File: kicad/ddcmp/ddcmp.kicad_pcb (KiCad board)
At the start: 2 copper layers, 29 parts, among them J1 UART, J2 BNC, J3 BNC, J4 LOOPTEST, U1 Pico, U2 max3089ecpd, U3 MAX3222, U4 MAX3222

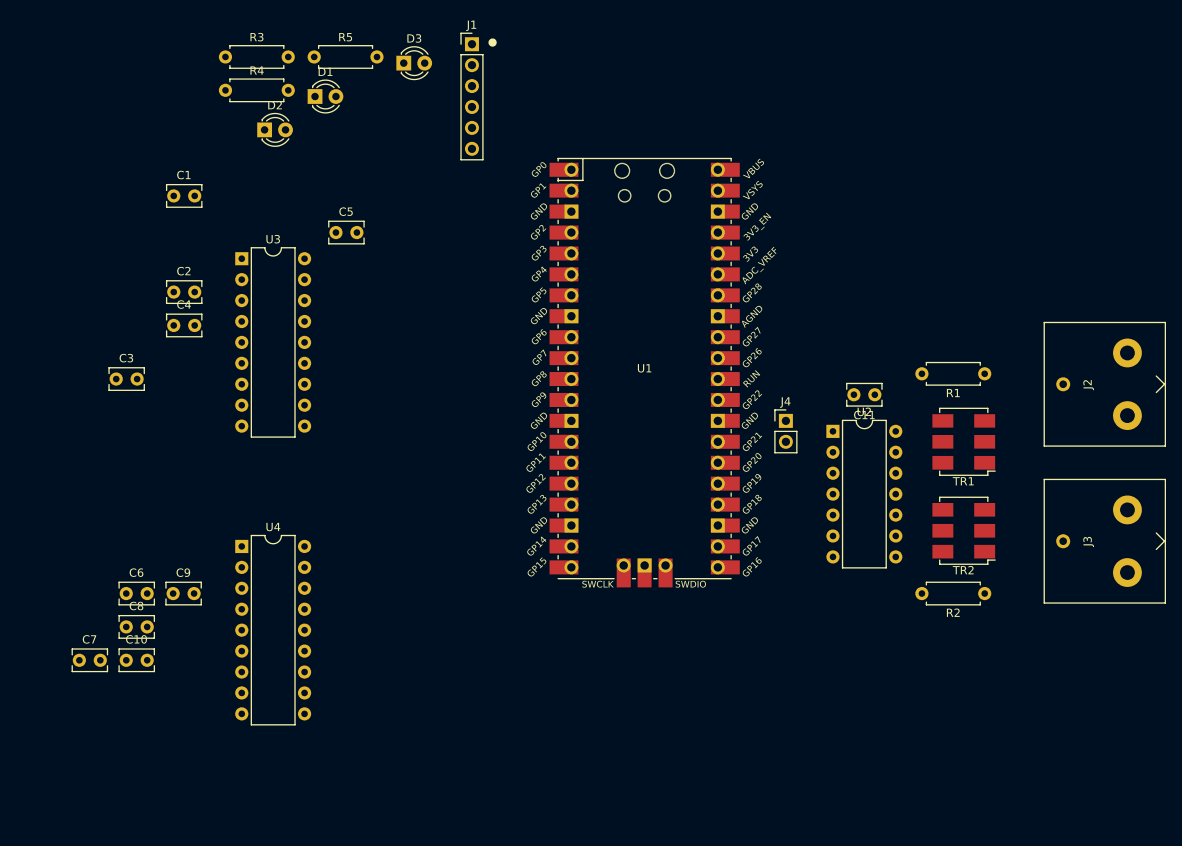
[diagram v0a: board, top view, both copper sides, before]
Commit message: Finish the connector hookups, to be verified carefully against DMR-11 schematics.
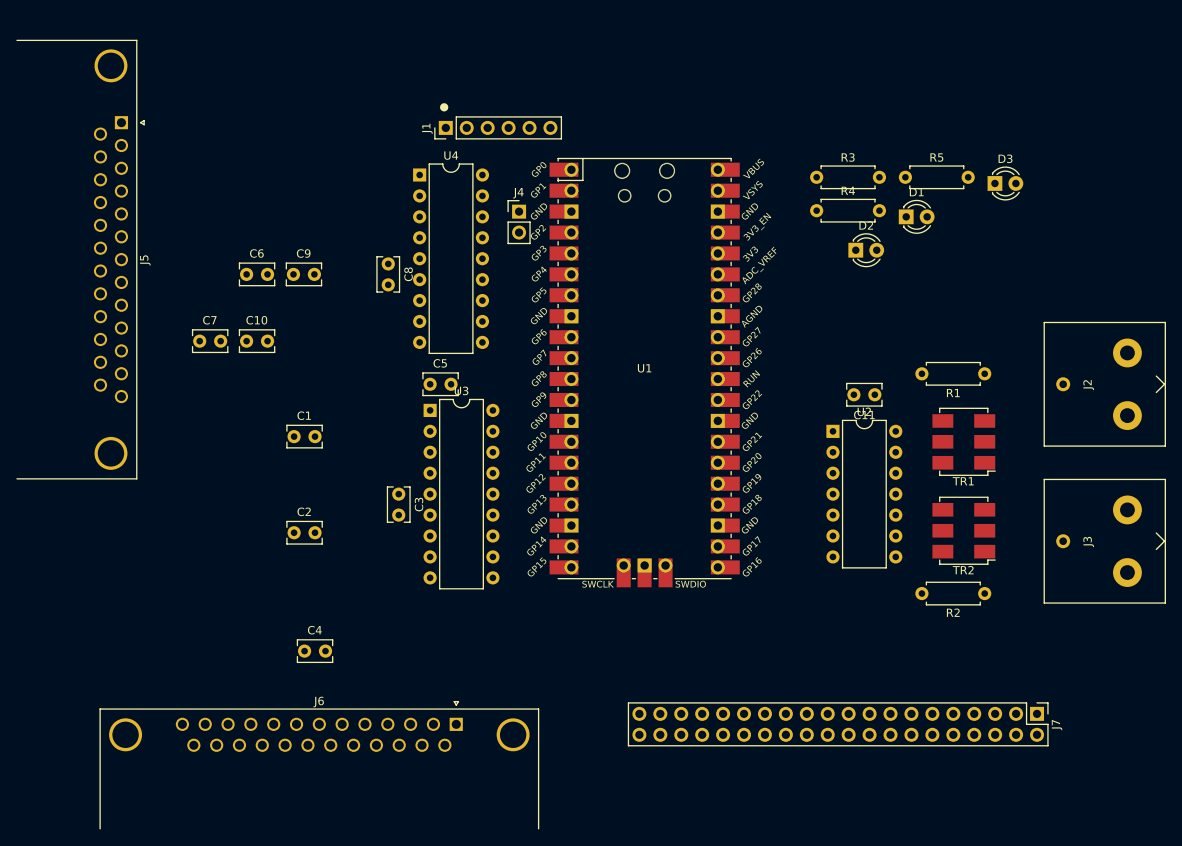
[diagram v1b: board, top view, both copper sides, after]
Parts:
- added J5: DTE, ddcmp_parts:Amphenol_DB25M_PCB, F.Cu at (29.2, 100.3)
- added J6: DCE, ddcmp_parts:Amphenol_DB25F_PCB, F.Cu at (69.8, 173.4)
- added J7: Bulkhead, ddcmp_parts:Berg_40_pin_DEC_pinout, F.Cu at (140.3, 172.1)
- J2: value BNC -> RX
- J3: value BNC -> TX
- moved D1 73.2 mm to (124.5, 111.8)
- moved D2 73.2 mm to (118.3, 115.8)
- moved D3 73.2 mm to (135.2, 107.7)
- moved R3 73.2 mm to (113.6, 107.0)
- moved R4 73.2 mm to (113.6, 111.0)
- moved R5 73.2 mm to (124.4, 107.0)
- moved C8 54.3 mm to (61.6, 117.5), turned to 270 degrees
- moved U4 50.0 mm to (65.4, 106.7)
- moved C4 42.6 mm to (51.4, 164.5)
- moved C10 41.4 mm to (44.4, 126.8)
- moved C7 41.4 mm to (38.7, 126.8)
- moved C9 41.4 mm to (50.1, 118.7)
- moved C6 41.4 mm to (44.4, 118.7)
- moved J4 41.2 mm to (77.5, 111.1)
- moved C3 37.0 mm to (62.9, 145.4), turned to 270 degrees
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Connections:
- net Net-(J2-Pad1) renamed /Integral modem/IM_RDX
- net Net-(J2-Pad2) renamed /Integral modem/IM_RXD_N
- net Net-(J3-Pad1) renamed /Integral modem/IM_TDX
- net Net-(J3-Pad2) renamed /Integral modem/IM_TXD_N
- TR2 pad 5: GND -> Net-(TR2-Pad5)
- U1 pad 12: /CPU/RS232_CLKEN -> Net-(U1-Pad12)
- U1 pad 21: /CPU/IM_RXDATA -> /CPU/IM_SRL
- U1 pad 25: /CPU/IM_SRL -> /CPU/IM_RXDATA
- U1 pad 26: Net-(U1-Pad26) -> Net-(D1-Pad2)
- U1 pad 27: Net-(J4-Pad2) -> Net-(D2-Pad2)
- U1 pad 29: Net-(U1-Pad29) -> Net-(D3-Pad2)
- U1 pad 4: Net-(D1-Pad2) -> Net-(J4-Pad2)
- U1 pad 5: Net-(D2-Pad2) -> Net-(U1-Pad5)
- U1 pad 6: Net-(D3-Pad2) -> Net-(U1-Pad6)
- U3 pad 14: Net-(U3-Pad14) -> /RS-232 I/O/RXD
- U3 pad 15: Net-(U3-Pad15) -> /RS-232 I/O/RS232_1
- U3 pad 8: Net-(U3-Pad8) -> /RS-232 I/O/TXD
- U4 pad 14: Net-(U4-Pad14) -> /RS-232 I/O/RXCLK
- U4 pad 15: Net-(U4-Pad15) -> /RS-232 I/O/CLKOUT
- U4 pad 18: /CPU/RS232_CLKEN -> /CPU/RS232_ENABLE
- U4 pad 8: Net-(U4-Pad8) -> /RS-232 I/O/RS232_0
- U4 pad 9: Net-(U4-Pad9) -> /RS-232 I/O/TXCLK

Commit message: Complete schematic, PCB layout, and matching code.  Needs testing.
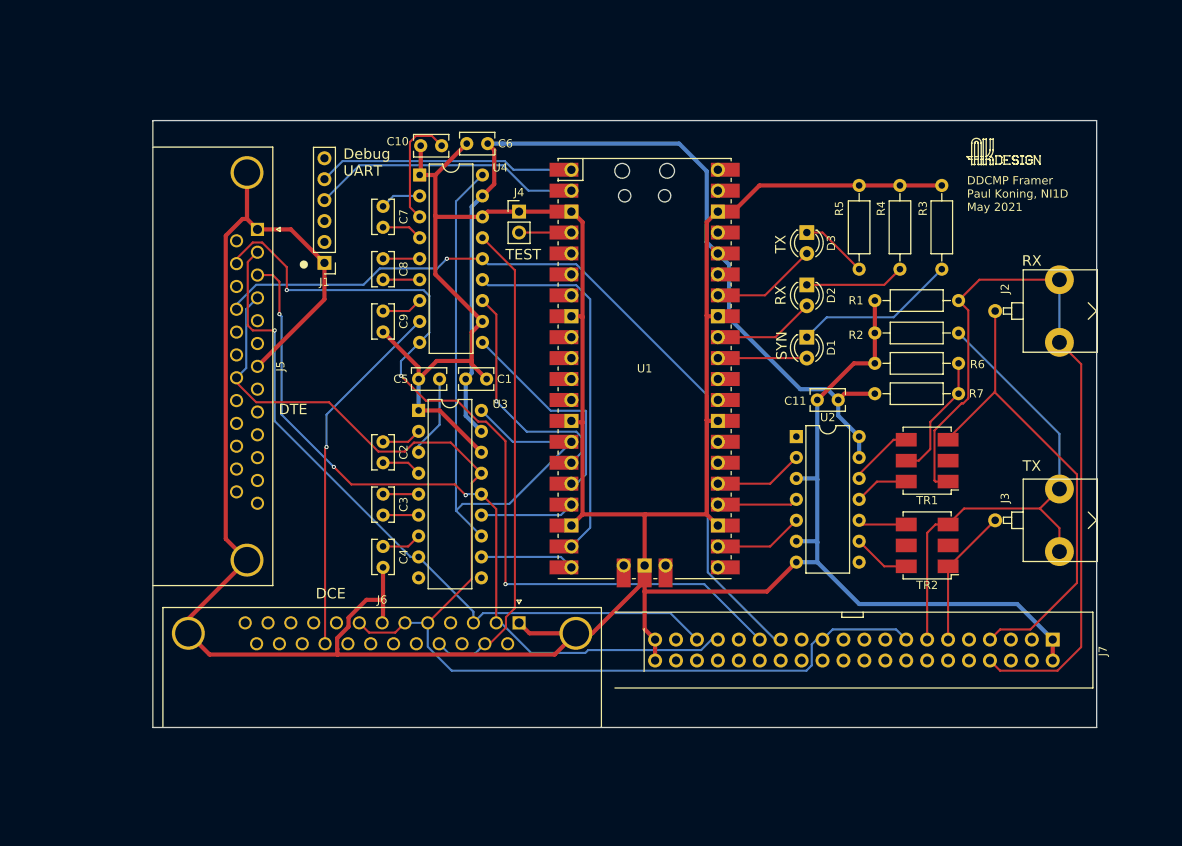
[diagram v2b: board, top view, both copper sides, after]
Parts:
- added R6: 240, ddcmp_parts:R_Axial_DIN0207_L6.3mm_D2.5mm_P10.16mm_Horizontal, F.Cu at (120.7, 133.2)
- added R7: 750, ddcmp_parts:R_Axial_DIN0207_L6.3mm_D2.5mm_P10.16mm_Horizontal, F.Cu at (130.8, 129.5)
- added REF**: AK_Design_9mm, ddcmp_parts:AK_Design_9mm, F.Cu at (131.8, 105.4)
- D1: value LED -> SYN; footprint LEDs:LED_D3.0mm -> ddcmp_parts:LED_D3.0mm
- D2: value LED -> RX; footprint LEDs:LED_D3.0mm -> ddcmp_parts:LED_D3.0mm
- D3: value LED -> TX; footprint LEDs:LED_D3.0mm -> ddcmp_parts:LED_D3.0mm
- J4: value LOOPTEST -> TEST; footprint Pin_Headers:Pin_Header_Straight_1x02_Pitch2.54mm -> ddcmp_parts:Pin_Header_Straight_1x02_Pitch2.54mm
- R1, R2, R3, R4, R5: footprint ddcmp_parts:R_Axial_DIN0207_L6.3mm_D2.5mm_P7.62mm_Horizontal -> ddcmp_parts:R_Axial_DIN0207_L6.3mm_D2.5mm_P10.16mm_Horizontal
- U2: value max3089ecpd -> max3491ecpd
- moved C10 33.5 mm to (68.1, 103.1), turned to 180 degrees
- moved C6 33.3 mm to (73.7, 102.9), turned to 180 degrees
- moved R2 31.8 mm to (130.8, 125.9)
- moved C7 27.6 mm to (61.0, 110.5), turned to 270 degrees
- moved D3 23.6 mm to (112.4, 113.7), turned to 270 degrees
- moved J1 22.0 mm to (53.8, 117.3), turned to 180 degrees
- moved C1 22.0 mm to (71.0, 131.4)
- moved J5 21.0 mm to (45.7, 113.3)
- moved D1 18.9 mm to (112.4, 126.4), turned to 270 degrees
- moved R3 18.8 mm to (128.8, 118.1), turned to 90 degrees
- moved C4 15.9 mm to (61.0, 151.8), turned to 270 degrees
- moved C2 15.4 mm to (61.0, 139.1), turned to 270 degrees
- moved J6 14.5 mm to (77.5, 161.0)
- moved R5 12.5 mm to (118.7, 118.1), turned to 90 degrees
- moved R4 12.4 mm to (123.7, 118.1), turned to 90 degrees
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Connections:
- J5 pad 15: /RS-232 I/O/CLKOUT -> /RS-232 I/O/TXCLK
- J5 pad 17: /RS-232 I/O/CLKOUT -> /RS-232 I/O/RXCLK
- J6 pad 15: /RS-232 I/O/TXCLK -> /RS-232 I/O/CLKOUT
- J6 pad 17: /RS-232 I/O/RXCLK -> /RS-232 I/O/CLKOUT
- U1 pad 21: /CPU/IM_SRL -> Net-(U1-Pad21)
- U1 pad 26: Net-(D1-Pad2) -> Net-(U1-Pad26)
- U1 pad 27: Net-(D2-Pad2) -> Net-(U1-Pad27)
- U1 pad 29: Net-(D3-Pad2) -> Net-(U1-Pad29)
- U1 pad 31: Net-(U1-Pad31) -> Net-(D1-Pad2)
- U1 pad 32: Net-(U1-Pad32) -> Net-(D2-Pad2)
- U1 pad 34: Net-(U1-Pad34) -> Net-(D3-Pad2)
- U2 pad 1: GND -> (no net)
- U2 pad 13: GND -> V3_3
- U2 pad 6: /CPU/IM_SRL -> GND
- U2 pad 8: GND -> (no net)
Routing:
- net GND: track 0.00 -> 504.6 mm
- net /RS-232 I/O/RS232_1: track 0.00 -> 142.9 mm
- net V3_3: track 0.00 -> 114.6 mm
- net /RS-232 I/O/TXCLK: track 0.00 -> 107.5 mm, vias 0 -> 3
- net /RS-232 I/O/RXCLK: track 0.00 -> 101.0 mm, vias 0 -> 1
- net /Integral modem/IM_RXD_N: track 0.00 -> 97.6 mm
- net /RS-232 I/O/RXD: track 0.00 -> 93.3 mm, vias 0 -> 3
- net /RS-232 I/O/TXD: track 0.00 -> 88.0 mm, vias 0 -> 1
- net /CPU/RS232_ENABLE: track 0.00 -> 76.4 mm
- net /Integral modem/IM_TXD_N: track 0.00 -> 61.4 mm
- net /RS-232 I/O/CLKOUT: track 0.00 -> 59.3 mm
- net /Integral modem/IM_RDX: track 0.00 -> 58.7 mm
- net /CPU/RS232_RXCLK: track 0.00 -> 45.0 mm
- net /RS-232 I/O/RS232_0: track 0.00 -> 43.9 mm, vias 0 -> 1
- net Net-(J1-Pad4): track 0.00 -> 33.0 mm
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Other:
- board outline added: 114.6 x 73.7 mm
- net class Default: clearance 0.2 -> 0.254; trace_width 0.25 -> 0.254; via_dia 0.8 -> 0.508; via_drill 0.4 -> 0.254
- net class Power added: clearance 0.254, trace_width 0.508, via_dia 0.508, via_drill 0.254
- rule pad_to_mask_clearance: 0 -> 0.0508
- rule trace_clearance: 0.2 -> 0.254
- rule trace_min: 0.2 -> 0.1524
- rule via_min_drill: 0.3 -> 0.254
- rule via_min_size: 0.4 -> 0.508
- board text added: "DCE"
- board text added: "DDCMP Framer Paul Koning, NI1D May 2021"
- board text added: "DTE"
- board text added: "Debug UART"
- board text added: "RX"
- board text added: "SYN"
- board text added: "TEST"
- board text added: "TX"

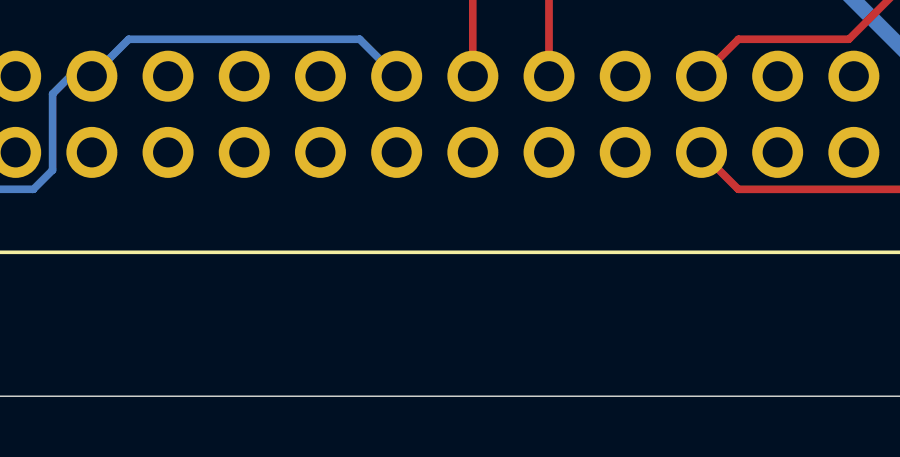
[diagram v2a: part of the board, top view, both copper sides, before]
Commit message: Schematics tweaks, better 3d model for RPico.
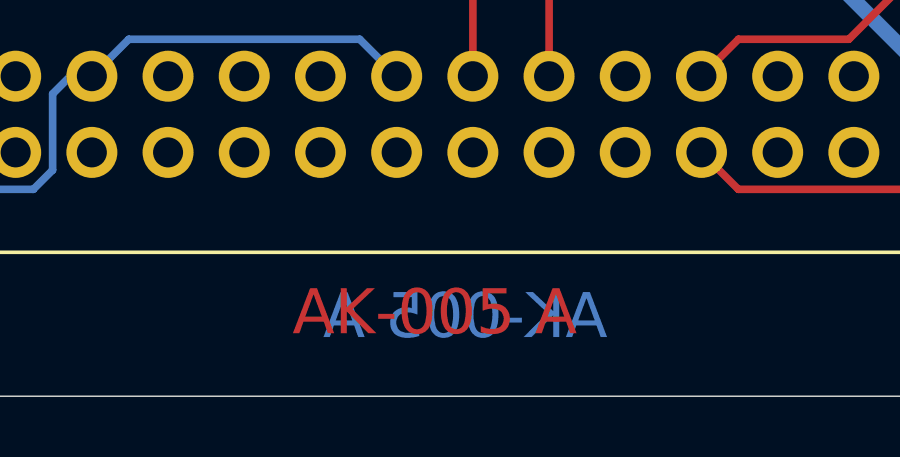
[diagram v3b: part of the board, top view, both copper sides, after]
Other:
- board text added: "AK-005 A"

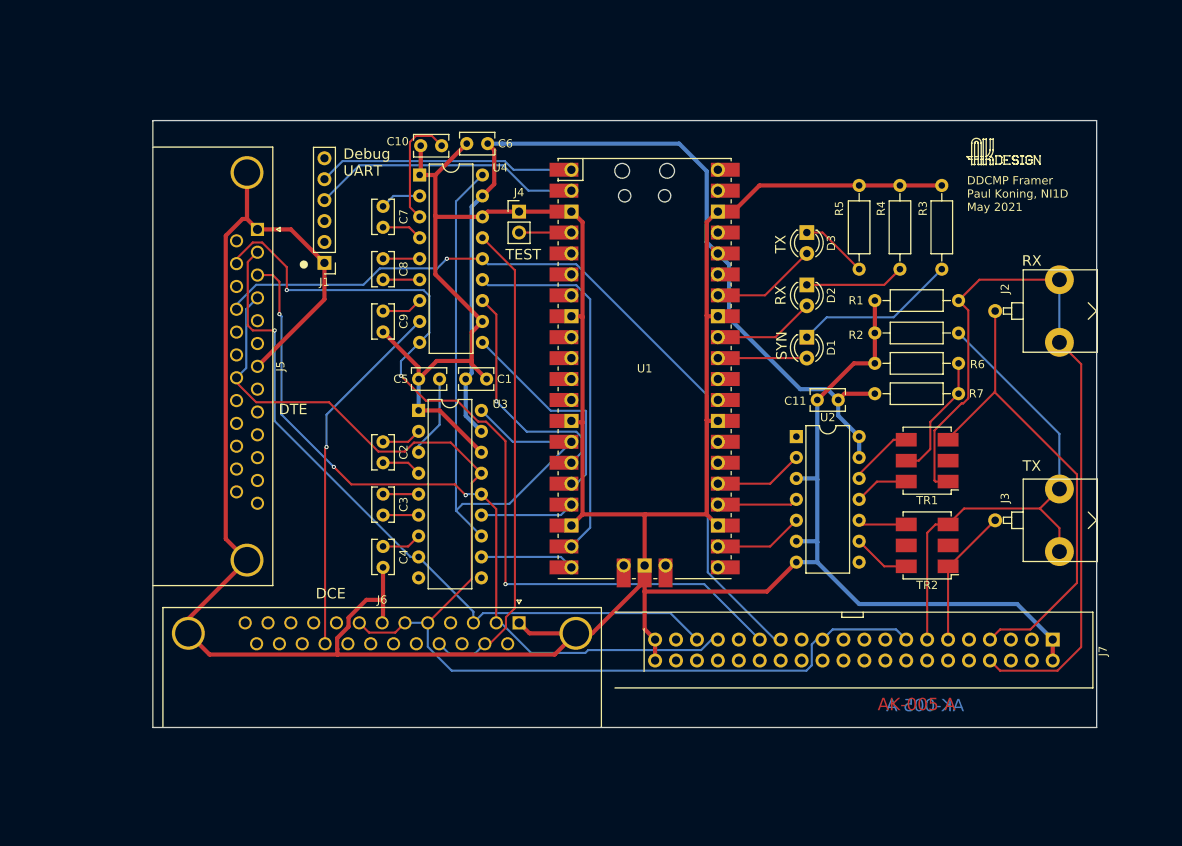
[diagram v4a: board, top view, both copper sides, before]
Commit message: Schematics and 3d model cleanups; first drafts of a lot of documentation.
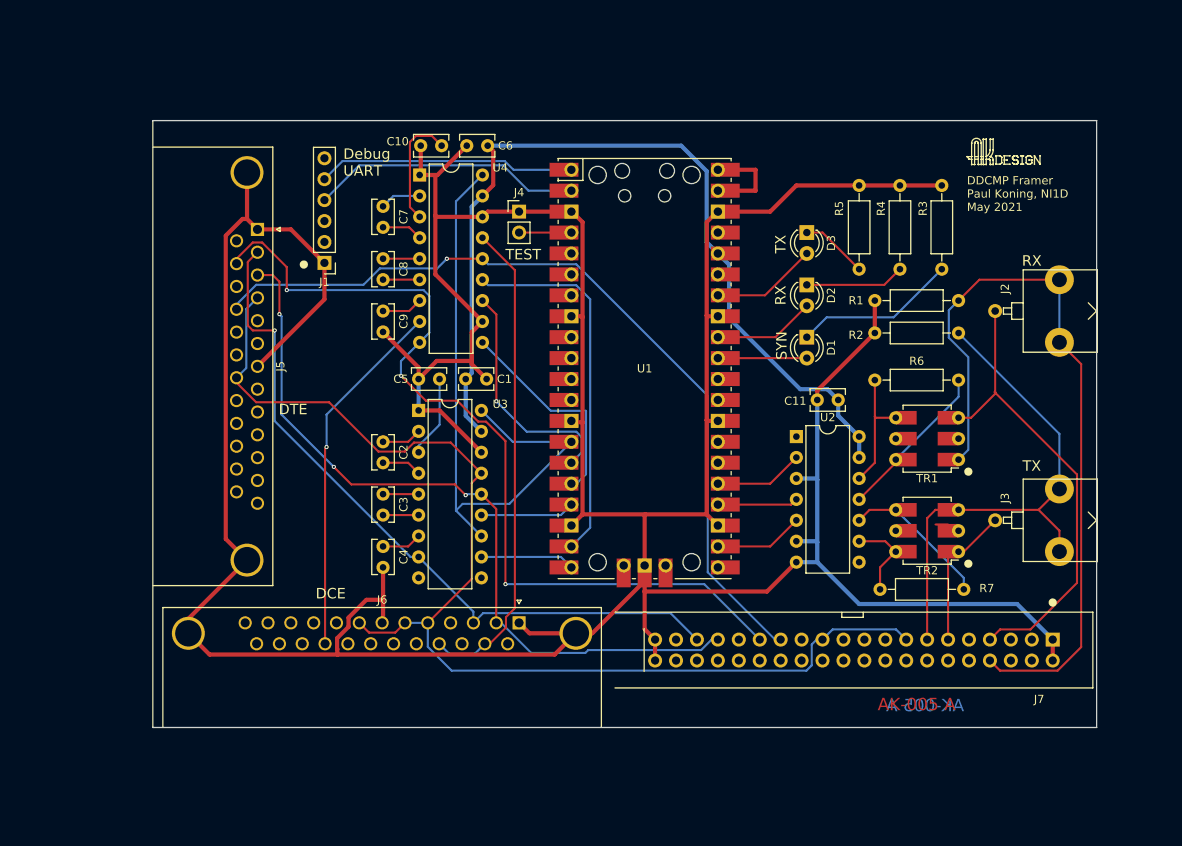
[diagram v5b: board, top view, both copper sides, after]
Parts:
- R6: value 240 -> 51
- R7: value 750 -> 51
- TR1, TR2: value ADT1-6T -> TT1-6-X65+; footprint ddcmp_parts:Mini-Circuits_CD637_H5.23mm -> ddcmp_parts:Mini-Circuits_CD637_X65
- moved R7 29.0 mm to (121.3, 157.0), turned to 0 degrees
- moved TR1 2.67 mm to (127.0, 138.7)
- moved TR2 1.78 mm to (127.0, 149.9)
- moved R6 1.65 mm to (120.7, 131.6)
- moved C6 0.25 mm to (73.7, 103.1)
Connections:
- R6 pad 1: V3_3 -> Net-(R6-Pad1)
- R7 pad 1: Net-(R6-Pad2) -> Net-(R7-Pad1)
- R7 pad 2: GND -> Net-(R7-Pad2)
- TR1 pad 2: (no net) -> Net-(TR1-Pad2)
- TR1 pad 4: Net-(TR1-Pad4) -> Net-(R6-Pad1)
- TR1 pad 5: Net-(R6-Pad2) -> Net-(TR1-Pad5)
- TR1 pad 6: Net-(TR1-Pad6) -> Net-(R6-Pad2)
- TR2 pad 2: (no net) -> Net-(TR2-Pad2)
- TR2 pad 4: Net-(TR2-Pad4) -> Net-(R7-Pad2)
- TR2 pad 6: Net-(TR2-Pad6) -> Net-(R7-Pad1)
- U1 pad 40: Net-(U1-Pad40) -> Net-(U1-Pad39)
- U2 pad 10: Net-(TR2-Pad4) -> Net-(R7-Pad2)
- U2 pad 11: Net-(TR1-Pad6) -> Net-(R6-Pad2)
- U2 pad 12: Net-(TR1-Pad4) -> Net-(R6-Pad1)
- U2 pad 9: Net-(TR2-Pad6) -> Net-(R7-Pad1)
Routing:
- net Net-(R7-Pad2): track 0.00 -> 19.3 mm
- net Net-(R6-Pad1): track 0.00 -> 17.1 mm
- net Net-(U1-Pad39): track 0.00 -> 11.7 mm
- net Net-(R7-Pad1): track 0.00 -> 10.3 mm
- net Net-(TR1-Pad4): track 7.96 -> 0.00 mm
- net Net-(TR2-Pad6): track 6.98 -> 0.00 mm
- net Net-(TR1-Pad6): track 6.61 -> 0.00 mm
- net Net-(TR2-Pad4): track 5.93 -> 0.00 mm
- net V3_3: track 114.6 -> 109.3 mm
- net Net-(R6-Pad2): track 15.3 -> 20.5 mm
- net /Integral modem/IM_RXD_N: track 97.6 -> 93.0 mm
- net Net-(TR2-Pad2): track 0.00 -> 1.52 mm
- net /Integral modem/IM_RDX: track 58.7 -> 57.6 mm
- net /Integral modem/IM_TDX: track 16.9 -> 18.0 mm
- net /Integral modem/IM_TXD_N: track 61.4 -> 62.4 mm
